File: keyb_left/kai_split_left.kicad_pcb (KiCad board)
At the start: 2 copper layers, 95.2 x 95.2 mm, 71 parts, among them J1 USB_C_Receptacle_USB2.0, J2 AudioJack4, SW1 SW_Push, U2 ATmega32U4-A, Y1 16MHz

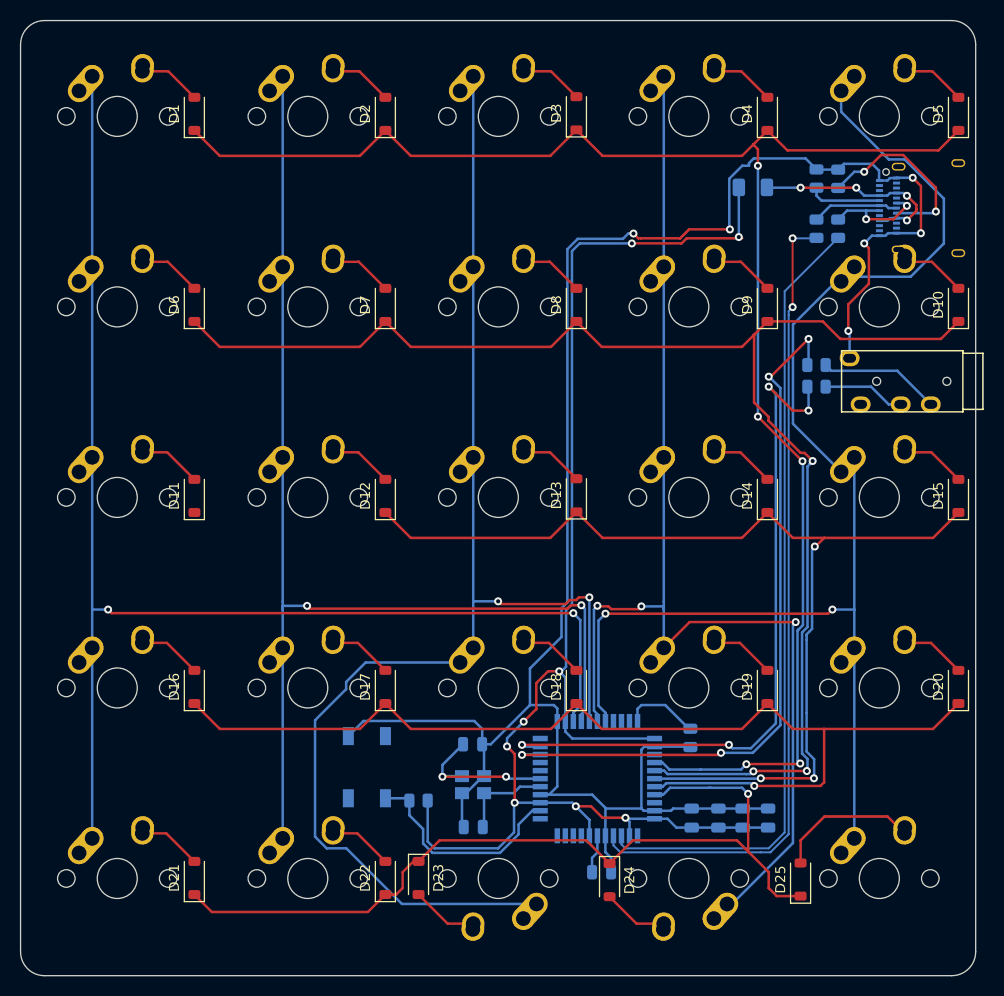
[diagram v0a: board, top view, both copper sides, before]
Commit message: basically done, only problem is that the quality is probably dog. Many other problems I can see too eg. the usb connector mounting point overlaps with a switch pole.
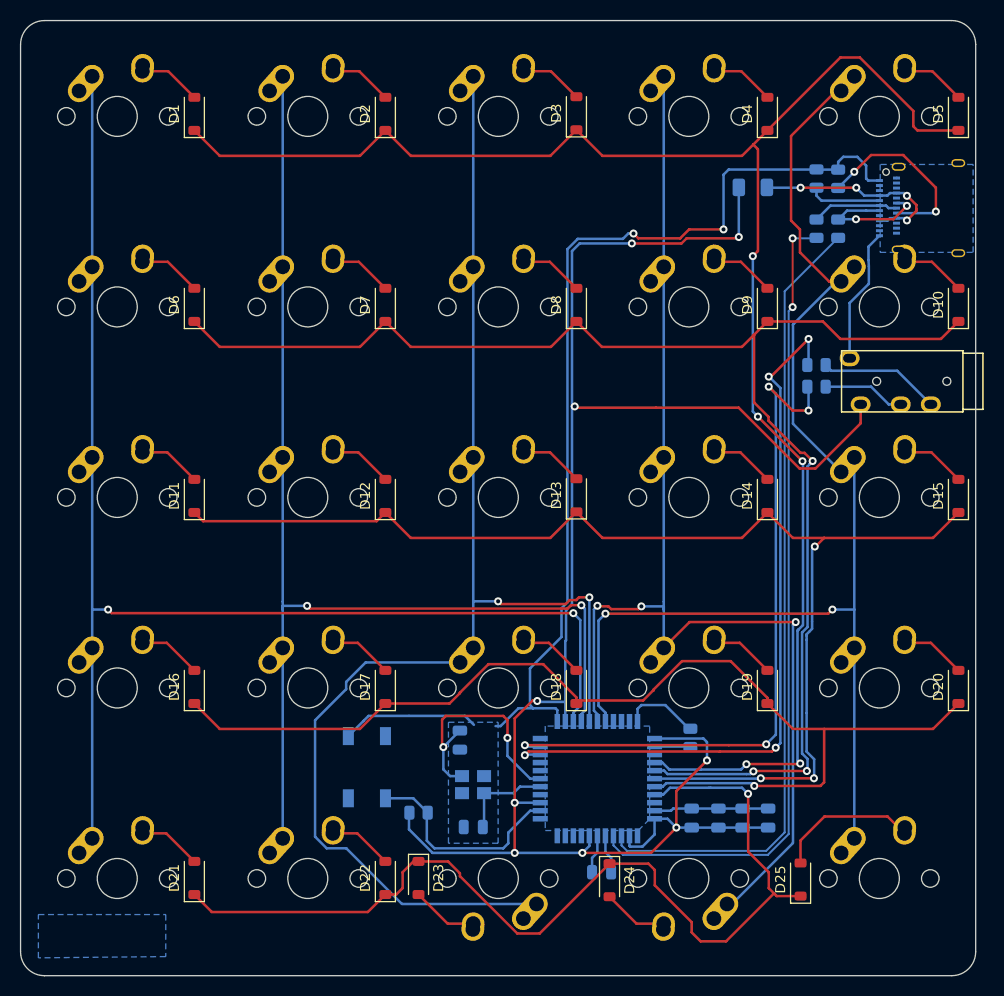
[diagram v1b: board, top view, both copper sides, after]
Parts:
- moved C7 1.33 mm to (66.0, 94.0), turned to 90 degrees
- moved R4 1.21 mm to (61.9, 101.2), turned to 0 degrees
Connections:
- J1 pad S1: unconnected-(J1-SHIELD-PadS1) -> Net-(D10-A)
- J2 pad 1: (no net) -> GND
- J2 pad 2: (no net) -> +5V
- J2 pad 3: (no net) -> Net-(J2-PadR1)
- J2 pad 4: (no net) -> Net-(J2-PadR2)
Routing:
- net GND: track 201.2 -> 143.2 mm, vias 6 -> 2
- net +5V: track 145.1 -> 190.6 mm, vias 8 -> 9
- net ROW2: track 104.5 -> 124.2 mm
- net ROW4: track 85.9 -> 97.9 mm
- net COL4: track 129.8 -> 121.7 mm
- net Net-(U2-XTAL1): track 16.1 -> 24.1 mm
- net ROW0: track 163.4 -> 169.1 mm
- net ROW3: track 107.2 -> 110.5 mm
- net Net-(J1-D--PadA7): track 11.1 -> 13.1 mm
- net TX: track 70.2 -> 69.4 mm
- net Net-(U2-~{RESET}): track 21.7 -> 21.0 mm
- added copper zone on B.Cu, net (none)
- added copper zone on B.Cu, net GND
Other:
- board text added: "Enter the cum zone"
